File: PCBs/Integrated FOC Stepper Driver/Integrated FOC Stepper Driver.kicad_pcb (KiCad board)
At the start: 2 copper layers, 42 x 42 mm, 63 parts, among them J1 INPUT, J2 USB C Receptacle, J3 OUTPUT, J4 MOTOR, J5 Conn_01x02, SW1 RESET, SW2 BOOT, U1 SE8650X2-HF, U2 SE8650X2-HF, U3 W25Q128JVS, U4 RP2040, U5 SN65HVD1050D, U6 MT6701CT, Y1 12MHz/12pF/50Ω/20ppm

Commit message: V1 of driver PCB
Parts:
- removed D4: D_Schottky, Diode_SMD:D_SMA_Handsoldering
- removed R15: 500, Resistor_SMD:R_0805_2012Metric_Pad1.20x1.40mm_HandSolder
- removed the U3 at (55.1, 55.2)
- added C25: 100nF, Capacitor_SMD:C_0402_1005Metric_Pad0.74x0.62mm_HandSolder, F.Cu at (41.7, 29.9)
- added C26: 100nF, Capacitor_SMD:C_0402_1005Metric_Pad0.74x0.62mm_HandSolder, B.Cu at (53.2, 52.0)
- added U4: W25Q128JVS, Package_SO:SOIC-8_5.23x5.23mm_P1.27mm, F.Cu at (61.0, 50.0)
- C10, C11, C12, C17, C3, C6, C7, C8: value 100n -> 100nF; footprint Capacitor_SMD:C_0603_1608Metric_Pad1.08x0.95mm_HandSolder -> Capacitor_SMD:C_0402_1005Metric_Pad0.74x0.62mm_HandSolder
- C13, C14: value 22p -> 100nF; footprint Capacitor_SMD:C_0603_1608Metric_Pad1.08x0.95mm_HandSolder -> Capacitor_SMD:C_0402_1005Metric_Pad0.74x0.62mm_HandSolder
- C15, C9: value 1u -> 100nF; footprint Capacitor_SMD:C_0603_1608Metric_Pad1.08x0.95mm_HandSolder -> Capacitor_SMD:C_0402_1005Metric_Pad0.74x0.62mm_HandSolder
- C16: value 100n -> 1u; footprint Capacitor_SMD:C_0603_1608Metric_Pad1.08x0.95mm_HandSolder -> Capacitor_SMD:C_0402_1005Metric_Pad0.74x0.62mm_HandSolder
- C18, C19: value 100n -> 22pF; footprint Capacitor_SMD:C_0603_1608Metric_Pad1.08x0.95mm_HandSolder -> Capacitor_SMD:C_0402_1005Metric_Pad0.74x0.62mm_HandSolder
- C20: value 47uF -> 1u; footprint Capacitor_SMD:C_0603_1608Metric_Pad1.08x0.95mm_HandSolder -> Capacitor_SMD:C_0402_1005Metric_Pad0.74x0.62mm_HandSolder
- C21: value 47uF -> 100nF; footprint Capacitor_SMD:C_0603_1608Metric_Pad1.08x0.95mm_HandSolder -> Capacitor_SMD:C_0402_1005Metric_Pad0.74x0.62mm_HandSolder
- C22, C23: value 100nF -> 47uF; footprint Capacitor_SMD:C_0603_1608Metric_Pad1.08x0.95mm_HandSolder -> Capacitor_SMD:C_2220_5750Metric_Pad1.97x5.40mm_HandSolder
- C24: footprint Capacitor_SMD:C_0603_1608Metric_Pad1.08x0.95mm_HandSolder -> Capacitor_SMD:C_0402_1005Metric_Pad0.74x0.62mm_HandSolder
- C4: value 1uF -> 10uF
- D1: value LED -> WS2812B; footprint LED_SMD:LED_0603_1608Metric_Pad1.05x0.95mm_HandSolder -> LED_SMD:LED_WS2812B_PLCC4_5.0x5.0mm_P3.2mm
- D3: value D_Schottky -> BAT54C; footprint Diode_SMD:D_SMA_Handsoldering -> Package_TO_SOT_SMD:SOT-23_Handsoldering
- J1, J3: footprint Connector_JST:JST_PH_S4B-PH-SM4-TB_1x04-1MP_P2.00mm_Horizontal -> Connector_JST:JST_PH_S4B-PH-K_1x04_P2.00mm_Horizontal
- R1: value 10k -> 523; footprint Resistor_SMD:R_0603_1608Metric_Pad0.98x0.95mm_HandSolder -> Resistor_SMD:R_0402_1005Metric_Pad0.72x0.64mm_HandSolder
- R10: value 1k -> 120; footprint Resistor_SMD:R_0603_1608Metric_Pad0.98x0.95mm_HandSolder -> Resistor_SMD:R_0402_1005Metric_Pad0.72x0.64mm_HandSolder
- R11: value 120 -> 5k; footprint Resistor_SMD:R_0603_1608Metric_Pad0.98x0.95mm_HandSolder -> Resistor_SMD:R_0402_1005Metric_Pad0.72x0.64mm_HandSolder
- R12, R3: footprint Resistor_SMD:R_0603_1608Metric_Pad0.98x0.95mm_HandSolder -> Resistor_SMD:R_0402_1005Metric_Pad0.72x0.64mm_HandSolder
- R13: value 5k -> 523; footprint Resistor_SMD:R_0603_1608Metric_Pad0.98x0.95mm_HandSolder -> Resistor_SMD:R_0402_1005Metric_Pad0.72x0.64mm_HandSolder
- R14: value 500 -> 523; footprint Resistor_SMD:R_0805_2012Metric_Pad1.20x1.40mm_HandSolder -> Resistor_SMD:R_0402_1005Metric_Pad0.72x0.64mm_HandSolder
- R2: value 500 -> 5.1k; footprint Resistor_SMD:R_0805_2012Metric_Pad1.20x1.40mm_HandSolder -> Resistor_SMD:R_0402_1005Metric_Pad0.72x0.64mm_HandSolder
- R4: value 5.1k -> 10k; footprint Resistor_SMD:R_0603_1608Metric_Pad0.98x0.95mm_HandSolder -> Resistor_SMD:R_0402_1005Metric_Pad0.72x0.64mm_HandSolder
- R5: value 1K -> 27.4; footprint Resistor_SMD:R_0603_1608Metric_Pad0.98x0.95mm_HandSolder -> Resistor_SMD:R_0402_1005Metric_Pad0.72x0.64mm_HandSolder
- R6: value 10K -> 27.4; footprint Resistor_SMD:R_0603_1608Metric_Pad0.98x0.95mm_HandSolder -> Resistor_SMD:R_0402_1005Metric_Pad0.72x0.64mm_HandSolder
- R7: value 10k -> 1K; footprint Resistor_SMD:R_0603_1608Metric_Pad0.98x0.95mm_HandSolder -> Resistor_SMD:R_0402_1005Metric_Pad0.72x0.64mm_HandSolder
- R8: value 27.4 -> 10k; footprint Resistor_SMD:R_0603_1608Metric_Pad0.98x0.95mm_HandSolder -> Resistor_SMD:R_0402_1005Metric_Pad0.72x0.64mm_HandSolder
- R9: value 27.4 -> 1k; footprint Resistor_SMD:R_0603_1608Metric_Pad0.98x0.95mm_HandSolder -> Resistor_SMD:R_0402_1005Metric_Pad0.72x0.64mm_HandSolder
- SW1: value RESET -> BOOT
- SW2: value BOOT -> RESET
- U1: value SE8650X2-HF -> PJ54M50SE; footprint Package_TO_SOT_SMD:SOT-23_Handsoldering -> Package_TO_SOT_SMD:SOT-23-5_HandSoldering
- U2: value SE8650X2-HF -> PJ9500M33SA; moved to F.Cu
- U5, U7, U8, Y1: moved to F.Cu
- moved D1 90.5 mm to (32.0, 42.0), turned to -90 degrees
- moved R3 83.6 mm to (29.9, 63.5), turned to -90 degrees
- moved R5 79.9 mm to (40.9, 54.7)
- moved R6 78.4 mm to (40.9, 53.7), turned to 180 degrees
- moved R1 76.3 mm to (33.6, 46.1)
- moved C14 71.2 mm to (43.6, 46.8), turned to -45 degrees
- moved R10 70.0 mm to (48.9, 60.9), turned to 90 degrees
- moved C15 69.4 mm to (44.3, 46.1), turned to -45 degrees
- moved R9 68.6 mm to (46.3, 46.0), turned to -45 degrees
- moved C1 67.8 mm to (38.3, 64.3), turned to -90 degrees
- moved R2 67.1 mm to (30.9, 63.5), turned to -90 degrees
- moved C8 66.4 mm to (44.8, 52.3), turned to 45 degrees
- moved C7 66.2 mm to (48.7, 56.3), turned to 45 degrees
- moved C19 65.5 mm to (44.8, 44.4), turned to -45 degrees
- moved C9 65.4 mm to (42.9, 47.5), turned to -45 degrees
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- renumbered U4 to U3
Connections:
- C10 pad 1: +3.3V -> GND
- C10 pad 2: GND -> +3.3V
- C13 pad 2: /XIN -> +3.3V
- C14 pad 2: Net-(C14-Pad2) -> +1V1
- C15 pad 1: +3.3V -> GND
- C15 pad 2: GND -> +1V1
- C17 pad 1: GND -> +3.3V
- C17 pad 2: +3.3V -> GND
- C18 pad 2: +1V1 -> /XIN
- C19 pad 2: +3.3V -> Net-(C19-Pad2)
- C20 pad 1: VBUS -> +3.3V
- C21 pad 1: VBUS -> +5V
- C22 pad 1: +3.3V -> VBUS
- C4 pad 1: Net-(D3-A) -> Net-(U1-VOUT)
- C6 pad 1: GND -> +3.3V
- C6 pad 2: +3.3V -> GND
- C9 pad 2: +1V1 -> +3.3V
- D1 pad 1: GND -> +3.3V
- D1 pad 2: Net-(D1-A) -> Net-(D1-DOUT)
- D2 pad 4: Net-(D2-DIN) -> Net-(D1-DOUT)
- D3 pad 1: +5V -> /VUSB
- D3 pad 2: Net-(D3-A) -> Net-(U1-VOUT)
- J2 pad A4: Net-(D4-A) -> /VUSB
- J2 pad A9: Net-(D4-A) -> /VUSB
- J2 pad B4: Net-(D4-A) -> /VUSB
- J2 pad B9: Net-(D4-A) -> /VUSB
- J4 pad 1: /A1 -> /A2
- J4 pad 2: /A2 -> /A1
- J4 pad 3: /B1 -> /B2
- J4 pad 4: /B2 -> /B1
- R1 pad 1: Net-(D1-A) -> Net-(D1-DIN)
- R1 pad 2: /LED -> /NEOPIXEL
- R10 pad 1: Net-(C14-Pad2) -> /CAN_L
- R10 pad 2: /XOUT -> Net-(J5-Pin_2)
- R11 pad 1: /CAN_L -> /SDA
- R11 pad 2: Net-(J5-Pin_2) -> +3.3V
- R12 pad 1: /SDA -> /SCL
- R13 pad 1: /SCL -> /A_CURRENT
- R13 pad 2: +3.3V -> GND
- R14 pad 1: /A_CURRENT -> /B_CURRENT
- R2 pad 1: /NEOPIXEL -> Net-(J2-CC2)
- R2 pad 2: Net-(D2-DIN) -> GND
- R3 pad 1: Net-(J2-CC2) -> Net-(J2-CC1)
- R4 pad 1: Net-(J2-CC1) -> +3.3V
- R4 pad 2: GND -> /RUN
- R5 pad 1: /~{USB_BOOT} -> /USB_D+
- R5 pad 2: /QSPI_SS -> /USB_DP
- R6 pad 1: /QSPI_SS -> /USB_DN
- R6 pad 2: +3.3V -> /USB_D-
- R7 pad 1: +3.3V -> /~{USB_BOOT}
- R7 pad 2: /RUN -> /QSPI_SS
- R8 pad 1: /USB_D+ -> /QSPI_SS
- R8 pad 2: Net-(U4-USB_DP) -> +3.3V
- R9 pad 1: Net-(U4-USB_DM) -> Net-(C19-Pad2)
- R9 pad 2: /USB_D- -> /XOUT
- SW1 pad 2: /RUN -> /~{USB_BOOT}
- SW2 pad 2: /~{USB_BOOT} -> /RUN
- U1 pad 1: GND -> VBUS
- U1 pad 2: Net-(D3-A) -> GND
- U3 pad 16: /LED -> unconnected-(U3-GPIO13-Pad16)
- U3 pad 46: Net-(U4-USB_DM) -> /USB_DN
- U3 pad 47: Net-(U4-USB_DP) -> /USB_DP
- U7 pad 9: (no net) -> GND
- U8 pad 9: (no net) -> GND
- Y1 pad 1: Net-(C14-Pad2) -> Net-(C19-Pad2)
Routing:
- net Net-(D1-DOUT): track 0.00 -> 75.8 mm, vias 0 -> 2
- net VBUS: track 0.00 -> 52.1 mm, vias 0 -> 13
- net +5V: track 0.00 -> 47.2 mm, vias 0 -> 3
- net /B_CURRENT: track 0.00 -> 36.0 mm, vias 0 -> 3
- net +1V1: track 0.00 -> 34.3 mm, vias 0 -> 4
- net /RUN: track 0.00 -> 29.3 mm, vias 0 -> 2
- net +3.3V: track 0.00 -> 29.0 mm, vias 0 -> 26
- net /B2: track 0.00 -> 28.4 mm, vias 0 -> 3
- net /A_CURRENT: track 0.00 -> 27.0 mm, vias 0 -> 2
- net /CAN_S: track 0.00 -> 26.8 mm, vias 0 -> 2
- net /A1: track 0.00 -> 25.8 mm, vias 0 -> 3
- net /CAN_H: track 0.00 -> 21.5 mm
- net /CAN_L: track 0.00 -> 20.7 mm, vias 0 -> 1
- net /USB_DP: track 0.00 -> 18.8 mm
- net /B1: track 0.00 -> 18.7 mm, vias 0 -> 3
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- added copper zone on F.Cu, net +3.3V
- added copper zone on In1.Cu, net +3.3V
- added copper zone on In2.Cu, net GND
- added copper zone on In4.Cu, net GND
- added copper zone on In3.Cu, net VBUS
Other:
- copper layers 2 -> 6
- board text added: "120TR"

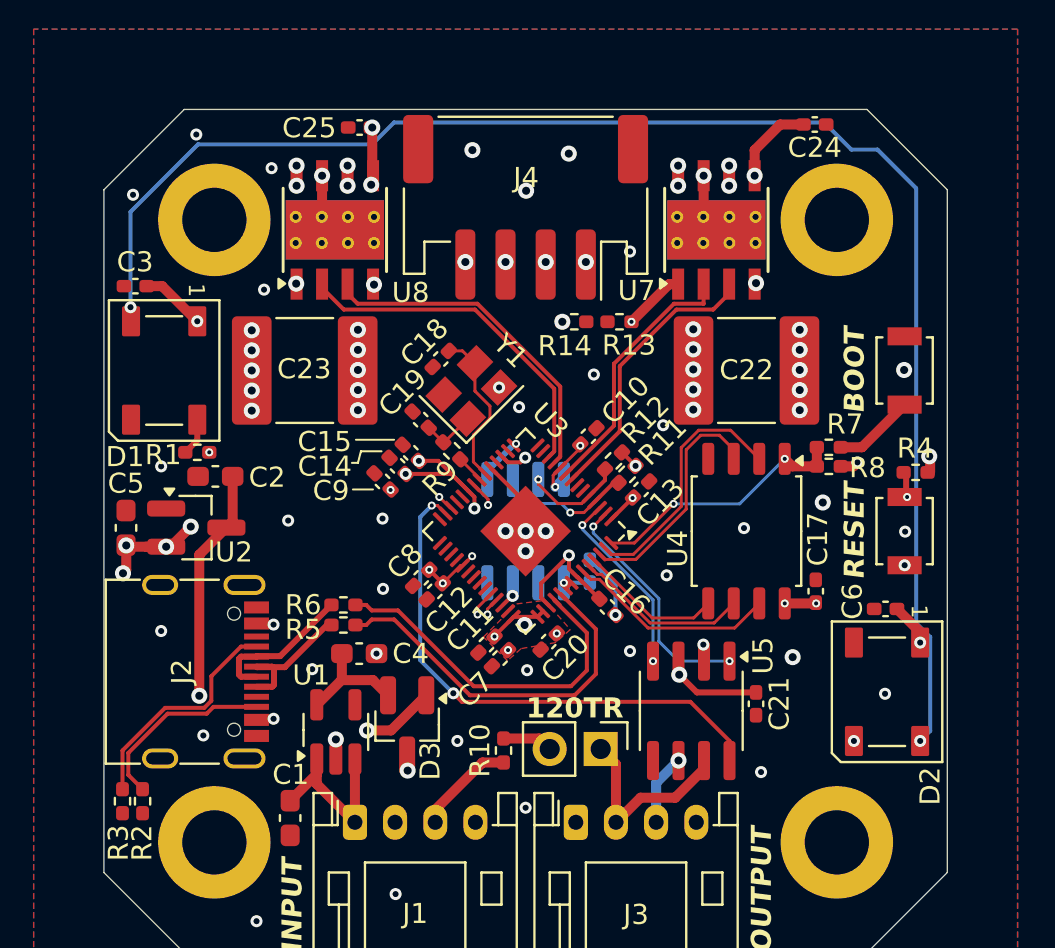
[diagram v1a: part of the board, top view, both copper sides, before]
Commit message: Update trace clearance
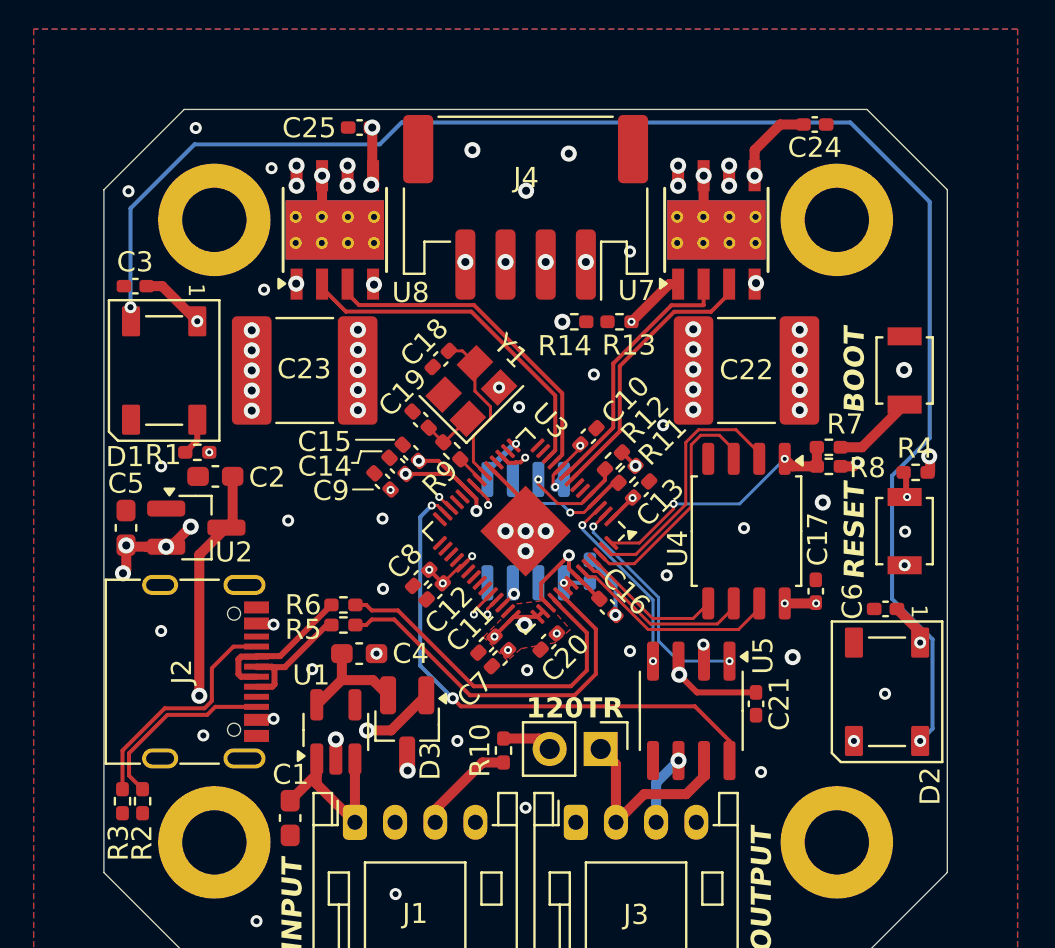
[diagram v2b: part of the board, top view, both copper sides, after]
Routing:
- net Net-(D1-DOUT): track 75.8 -> 77.6 mm

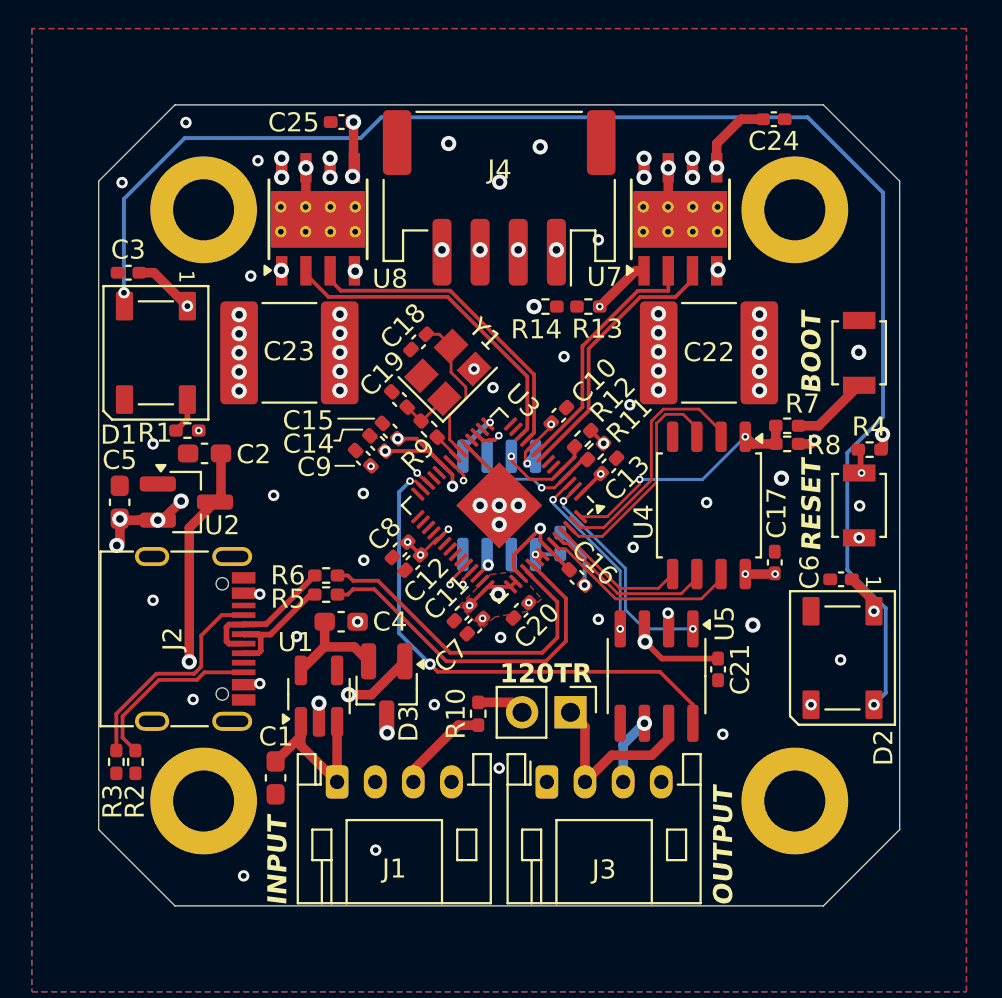
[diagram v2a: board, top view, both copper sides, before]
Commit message: Clean up schematic, remove all 0.4/0.2mm vias from layout
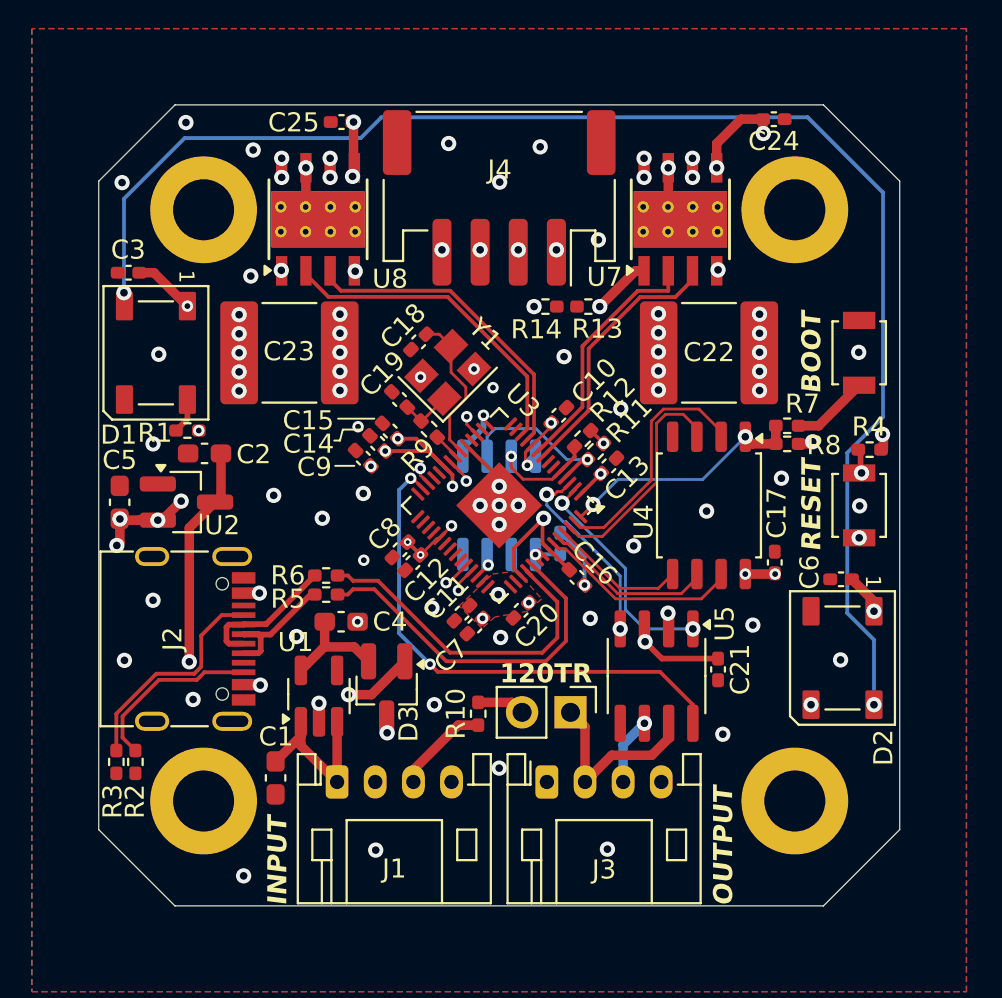
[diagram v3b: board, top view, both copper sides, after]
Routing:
- net +3.3V: track 29.0 -> 26.4 mm, vias 26 -> 25
- net /NEOPIXEL: track 18.4 -> 16.1 mm
- net +1V1: track 34.5 -> 36.6 mm
- net /SDA: track 6.89 -> 8.75 mm
- net VBUS: track 52.4 -> 53.2 mm, vias 13 -> 14
- net /CAN_RX: track 9.47 -> 10.2 mm
- net Net-(D1-DOUT): track 77.6 -> 77.0 mm
- net GND: vias 55 -> 63

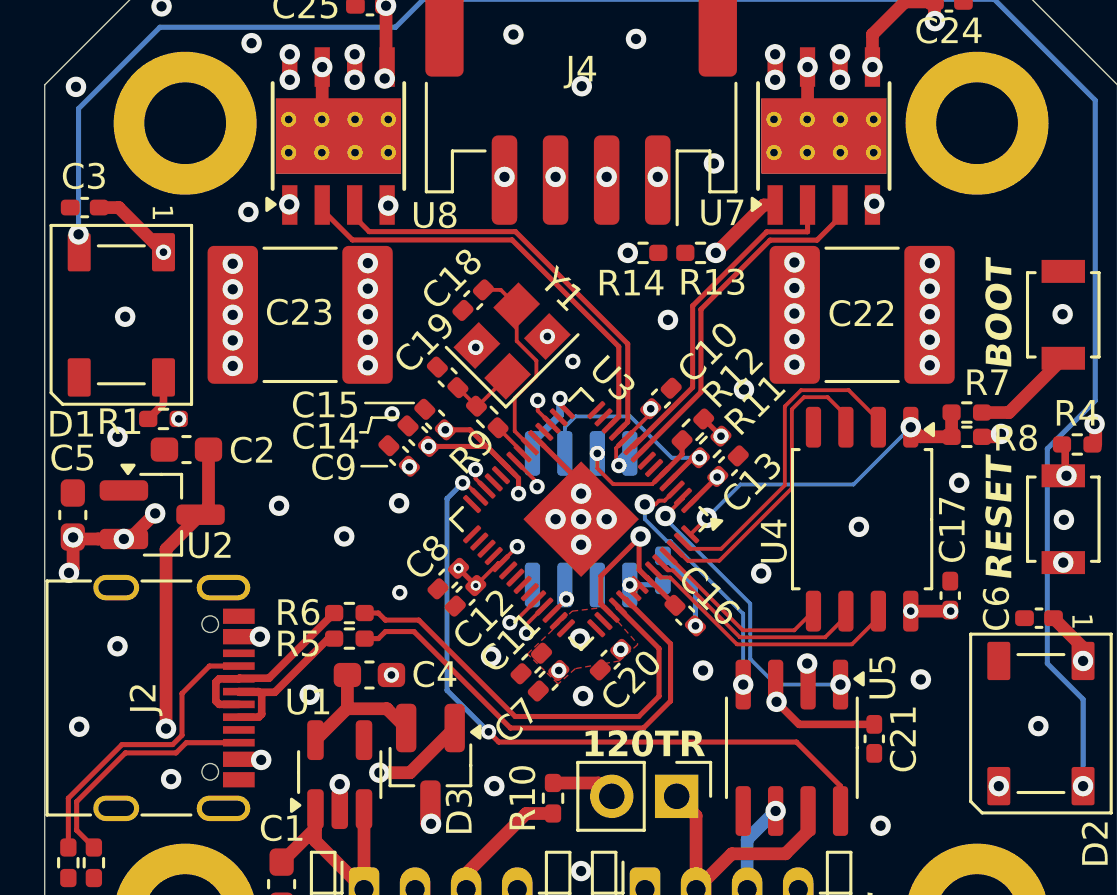
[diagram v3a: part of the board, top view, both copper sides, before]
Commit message: Remove all 0.6/0.3mm vias and add HV keep-out zone around MCU
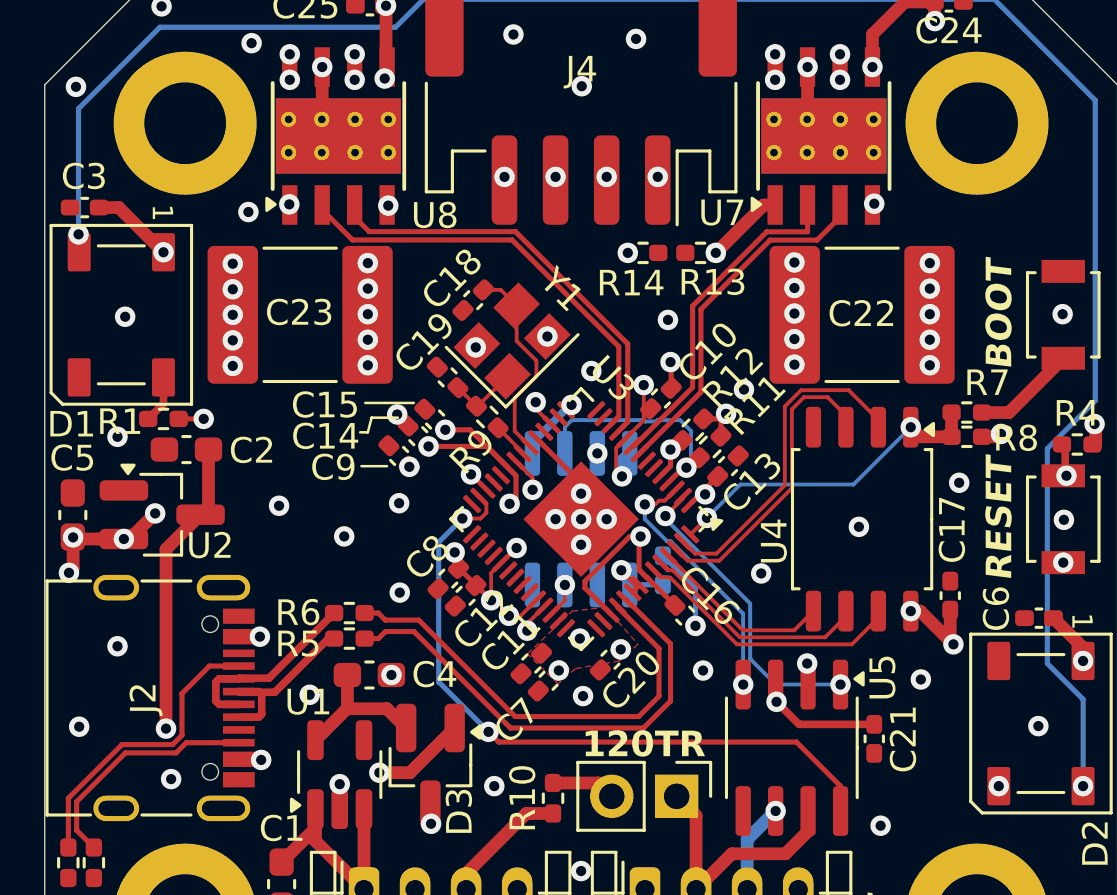
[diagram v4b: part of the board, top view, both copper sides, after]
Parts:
- R7: value 1K -> 1k
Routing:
- net +3.3V: track 26.4 -> 34.8 mm
- net +1V1: track 36.6 -> 38.4 mm
- net /SCL: track 5.18 -> 4.08 mm, vias 1 -> 2
- net GND: track 12.1 -> 13.1 mm, vias 63 -> 62
- net /SDA: track 8.75 -> 9.42 mm
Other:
- board text added: "+3.3V"
- board text added: "DIFFERENTIAL"
- board text added: "GND"
- board text added: "ROUTED"
- board text added: "VBUS"
